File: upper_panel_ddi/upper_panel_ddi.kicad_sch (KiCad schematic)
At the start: 32 parts, among them J1 Conn_01x05_Pin, J10 Conn_01x03_Pin, J11 Conn_01x03_Pin, J12 Conn_01x03_Pin, J2 Conn_01x10_Pin, J3 Conn_01x08_Pin, J4 Conn_01x10_Socket, J5 Conn_01x08_Pin, J6 Conn_01x08_Pin, J7 Conn_01x08_Pin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

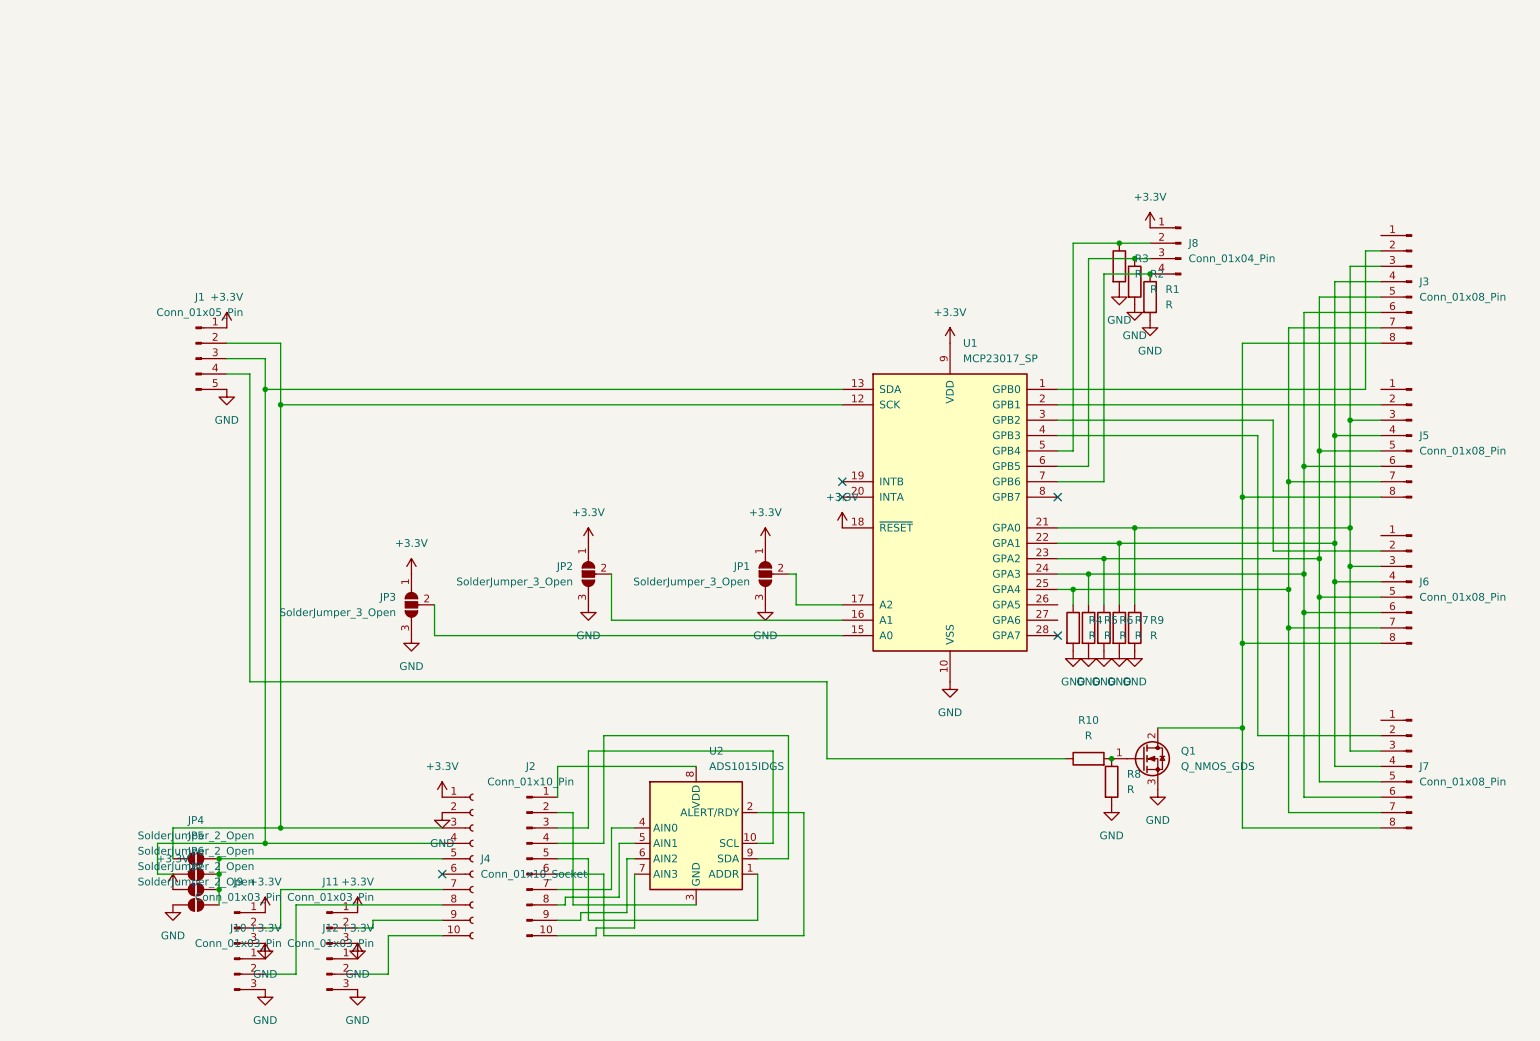
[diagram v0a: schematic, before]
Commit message: kicad: upper_panel_ddiを更新
IOエキスパンダを使わずRaspberry PI Picoを直接使うように
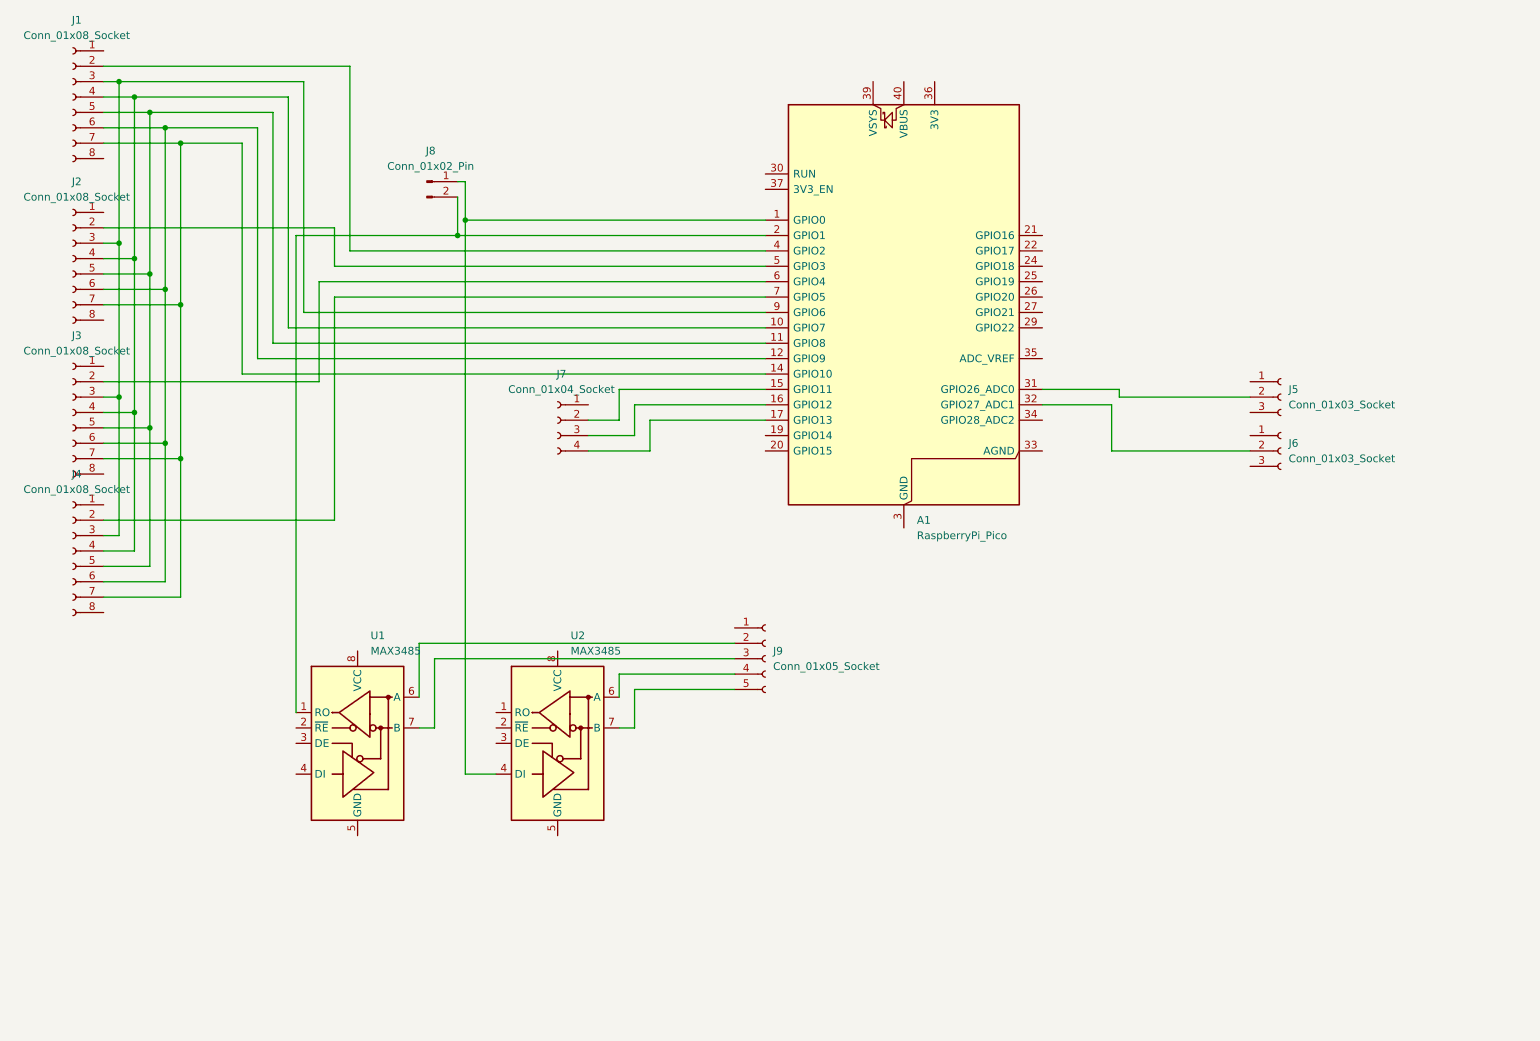
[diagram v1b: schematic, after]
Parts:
- removed J1: Conn_01x05_Pin, symbol Connector:Conn_01x05_Pin
- removed J10, J11, J12, J9: Conn_01x03_Pin, symbol Connector:Conn_01x03_Pin
- removed J2: Conn_01x10_Pin, symbol Connector:Conn_01x10_Pin
- removed J3, J5, J6, J7: Conn_01x08_Pin, symbol Connector:Conn_01x08_Pin
- removed J4: Conn_01x10_Socket, symbol Connector:Conn_01x10_Socket
- removed J8: Conn_01x04_Pin, symbol Connector:Conn_01x04_Pin
- removed JP1, JP2, JP3: SolderJumper_3_Open, symbol Jumper:SolderJumper_3_Open
- removed JP4, JP5, JP6, JP7: SolderJumper_2_Open, symbol Jumper:SolderJumper_2_Open
- removed Q1: Q_NMOS_GDS, symbol Transistor_FET:Q_NMOS_GDS
- removed R1, R10, R2, R3, R4, R5, R6, R7, R8, R9: R, symbol Device:R
- removed U1: MCP23017_SP, Package_DIP:DIP-28_W7.62mm, symbol Interface_Expansion:MCP23017_SP
- removed U2: ADS1015IDGS, Package_SO:TSSOP-10_3x3mm_P0.5mm, symbol Analog_ADC:ADS1015IDGS
- added A1: RaspberryPi_Pico, Module:RaspberryPi_Pico_Common_THT, symbol MCU_Module:RaspberryPi_Pico
- added J1, J2, J3, J4: Conn_01x08_Socket, Connector_JST:JST_ZH_B8B-ZR_1x08_P1.50mm_Vertical, symbol Connector:Conn_01x08_Socket
- added J5, J6: Conn_01x03_Socket, Connector_JST:JST_ZH_B3B-ZR_1x03_P1.50mm_Vertical, symbol Connector:Conn_01x03_Socket
- added J7: Conn_01x04_Socket, Connector_JST:JST_XH_B4B-XH-AM_1x04_P2.50mm_Vertical, symbol Connector:Conn_01x04_Socket
- added J8: Conn_01x02_Pin, Connector_PinHeader_2.54mm:PinHeader_1x02_P2.54mm_Vertical, symbol Connector:Conn_01x02_Pin
- added J9: Conn_01x05_Socket, Connector_JST:JST_XH_B5B-XH-AM_1x05_P2.50mm_Vertical, symbol Connector:Conn_01x05_Socket
- added U1, U2: MAX3485, Package_SO:SOIC-8_3.9x4.9mm_P1.27mm, symbol Interface_UART:MAX3485
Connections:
- new net: A1.1 (GPIO0), J8.1 (Pin_1), U2.4 (DI)
- new net: A1.10 (GPIO7), J1.4 (Pin_4), J2.4 (Pin_4), J3.4 (Pin_4), J4.4 (Pin_4)
- new net: A1.11 (GPIO8), J1.5 (Pin_5), J2.5 (Pin_5), J3.5 (Pin_5), J4.5 (Pin_5)
- new net: A1.12 (GPIO9), J1.6 (Pin_6), J2.6 (Pin_6), J3.6 (Pin_6), J4.6 (Pin_6)
- new net: A1.13 (GND), A1.18 (GND), A1.23 (GND), A1.28 (GND), A1.3 (GND), A1.38 (GND), A1.8 (GND)
- new net: A1.14 (GPIO10), J1.7 (Pin_7), J2.7 (Pin_7), J3.7 (Pin_7), J4.7 (Pin_7)
- new net: A1.15 (GPIO11), J7.2 (Pin_2)
- new net: A1.16 (GPIO12), J7.3 (Pin_3)
- new net: A1.17 (GPIO13), J7.4 (Pin_4)
- new net: A1.2 (GPIO1), J8.2 (Pin_2), U1.1 (RO)
- new net: A1.31 (GPIO26_ADC0), J5.2 (Pin_2)
- new net: A1.32 (GPIO27_ADC1), J6.2 (Pin_2)
- new net: A1.4 (GPIO2), J1.2 (Pin_2)
- new net: A1.5 (GPIO3), J2.2 (Pin_2)
- new net: A1.6 (GPIO4), J3.2 (Pin_2)
- new net: A1.7 (GPIO5), J4.2 (Pin_2)
- new net: A1.9 (GPIO6), J1.3 (Pin_3), J2.3 (Pin_3), J3.3 (Pin_3), J4.3 (Pin_3)
- new net: J9.2 (Pin_2), U1.6 (A)
- new net: J9.3 (Pin_3), U1.7 (B)
- new net: J9.4 (Pin_4), U2.6 (A)
- new net: J9.5 (Pin_5), U2.7 (B)
- no-connect marks 5 -> 0
